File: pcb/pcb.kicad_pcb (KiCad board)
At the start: 2 copper layers, 31.6 x 11.5 mm, 38 parts, among them IC1 ATMEGA32U2, Y1 MT 16MHz

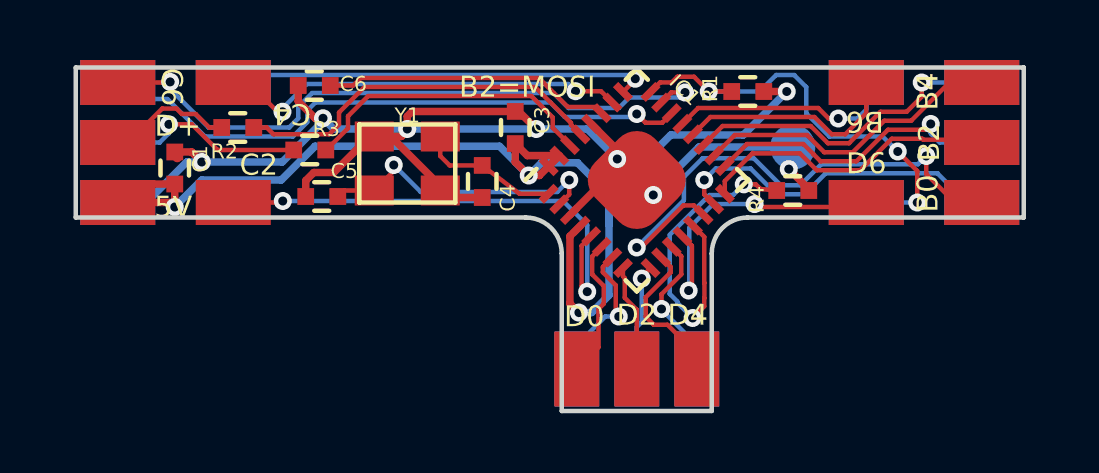
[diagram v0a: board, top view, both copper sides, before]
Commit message: Adapt to manufacturer's capabilities
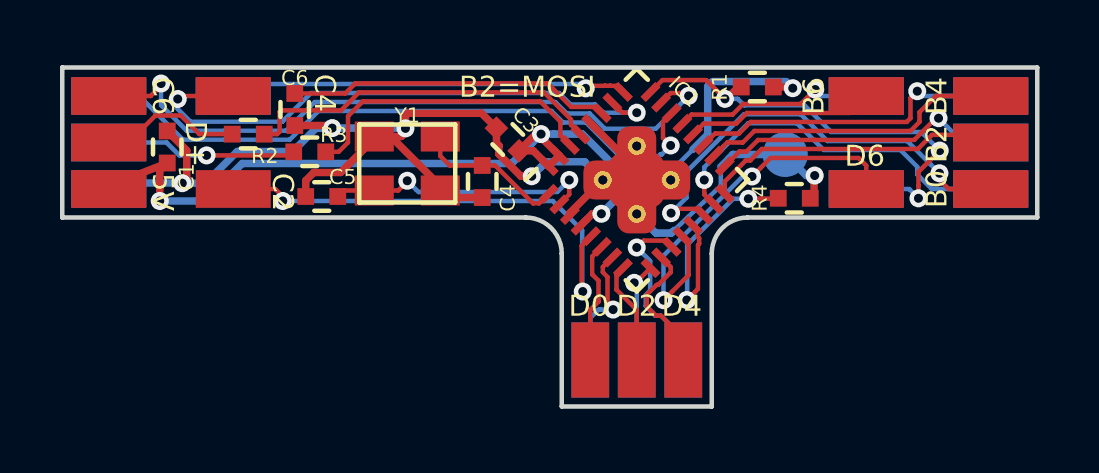
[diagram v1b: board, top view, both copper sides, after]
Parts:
- moved C6 1.03 mm to (138.6, 87.7), turned to 90 degrees
- moved C1 0.74 mm to (134.3, 88.9)
- moved W0 0.54 mm to (161.8, 90.3)
- moved W1 0.54 mm to (161.8, 90.3)
- moved W15 0.54 mm to (161.8, 87.2)
- moved W16 0.54 mm to (161.8, 87.2)
- moved W29 0.54 mm to (132.4, 87.2)
- moved W30 0.54 mm to (132.4, 87.2)
- moved W6 0.54 mm to (132.4, 90.3)
- moved W7 0.54 mm to (132.4, 90.3)
- moved W19 0.54 mm to (148.4, 96.0)
- moved W20 0.54 mm to (148.4, 96.0)
- moved W23 0.54 mm to (151.6, 96.0)
- moved W24 0.54 mm to (151.6, 96.0)
- moved C3 0.47 mm to (145.7, 88.7), turned to 135 degrees
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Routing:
- net VCC: track 42.8 -> 35.5 mm
- net /C4: track 13.7 -> 19.3 mm
- net GND: track 49.3 -> 52.7 mm, vias 7 -> 5
- net /B0: track 18.1 -> 14.9 mm
- net Net-(IC1-Pad13): track 10.8 -> 8.26 mm
- net /D6: track 11.0 -> 13.0 mm
- net /C5: track 14.7 -> 13.3 mm
- net /B6: track 7.86 -> 6.60 mm
- net /C7: track 20.7 -> 22.0 mm
- net /C6: track 21.7 -> 22.9 mm
- net Net-(C6-Pad2): track 9.64 -> 10.8 mm
- net /B1: track 11.6 -> 12.6 mm
- net /D5: track 4.96 -> 5.98 mm
- net /B7: track 7.70 -> 6.87 mm
- net /B3: track 10.1 -> 10.8 mm
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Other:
- board size 31.6 x 11.5 mm -> 32.5 x 11.3 mm
